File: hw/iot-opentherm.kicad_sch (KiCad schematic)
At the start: 32 parts, among them J1 USB_B_Micro, J2 Conn_01x02, J3 Conn_01x03, J4 Conn_02x06_Odd_Even, J5 Conn_01x02, Q1 BC858, U1 AMS1117-3.3, U2 ESP-12S, U3 PC817, U4 PC817

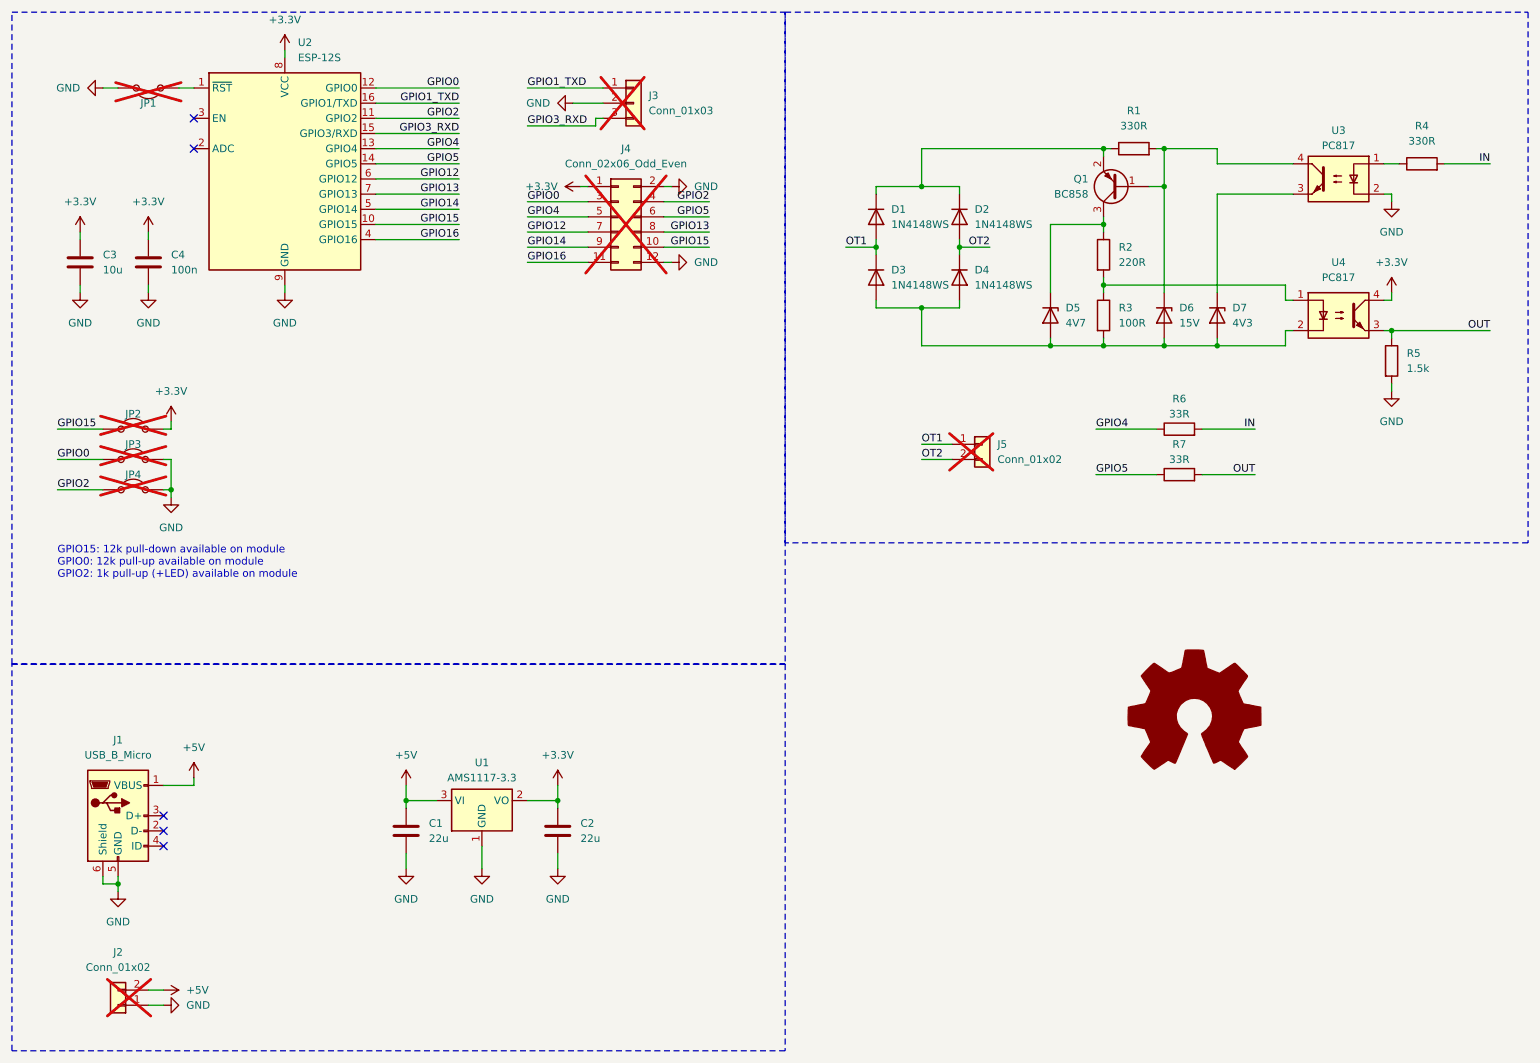
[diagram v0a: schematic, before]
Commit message: Fixes after running first version
1. Corrected footprint for D1, D2, D3, D4 to bigger one
2. Added connectors for OTx and +5VDC.
3. Added labels for OTx and +5VDC
4. ERC: no regression
5. DRC: two more issues
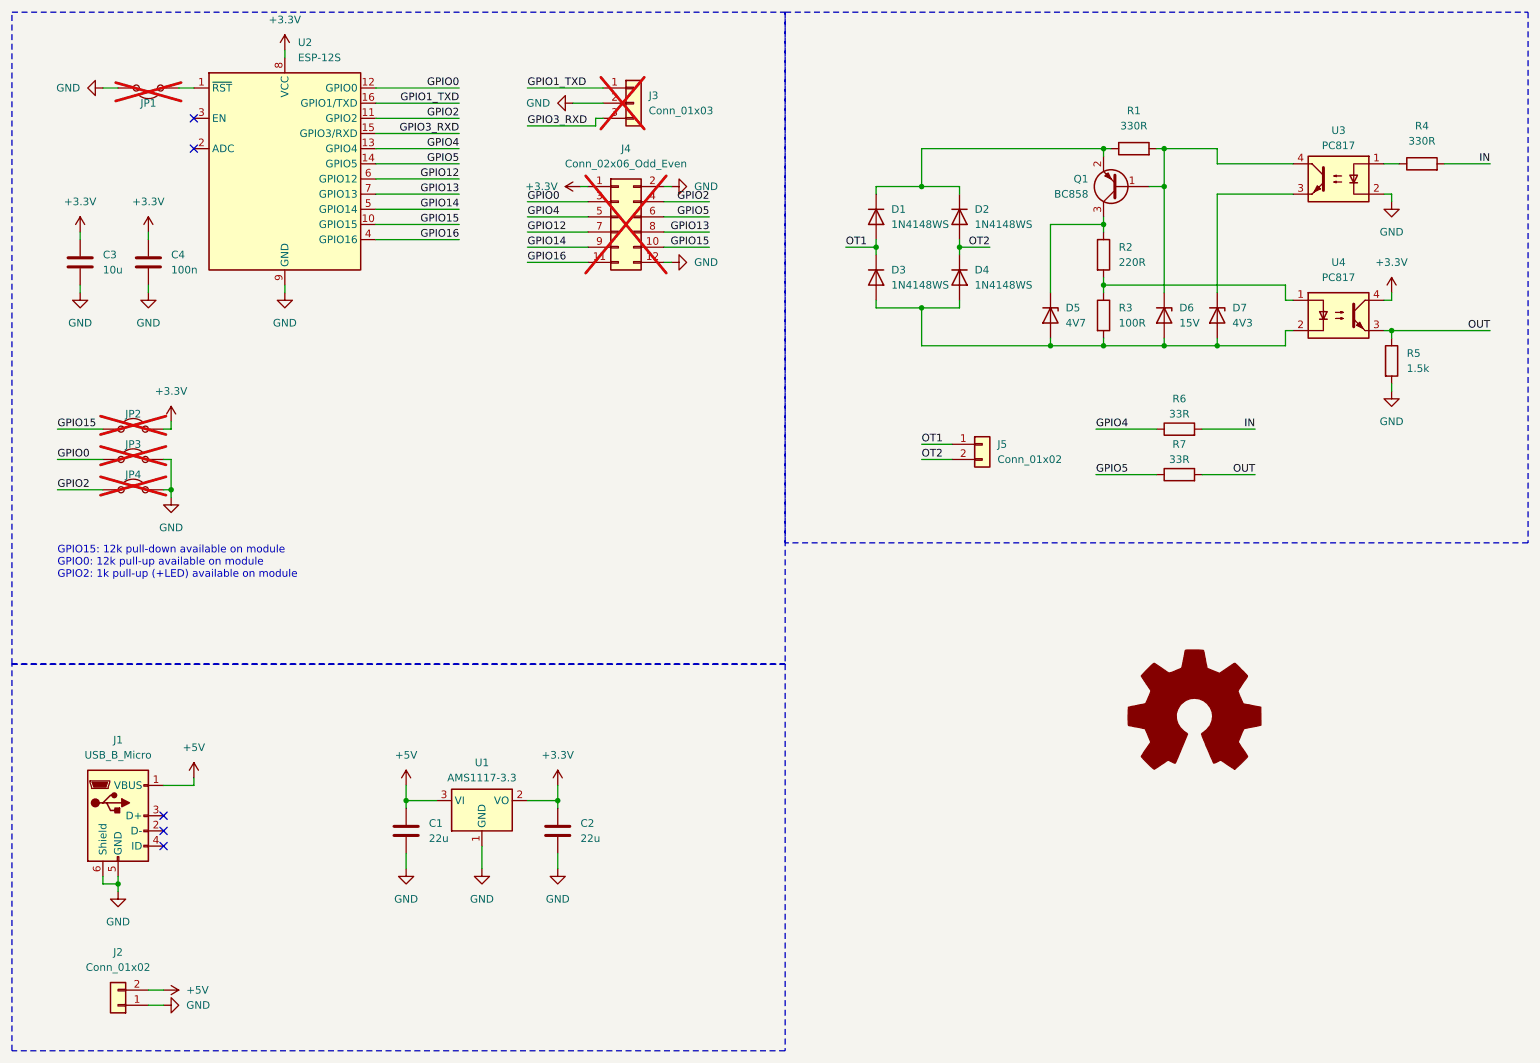
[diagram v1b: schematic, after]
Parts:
- D1, D2, D3, D4: footprint Diode_SMD:D_SOD-323 -> Diode_SMD:D_SOD-323_HandSoldering
- J2, J5: footprint Connector_PinHeader_2.54mm:PinHeader_1x02_P2.54mm_Vertical -> Connector_TE-Connectivity_:TE_282834-2; Farnell (none) -> 2112482; LCSC (none) -> C592983; Mouser (none) -> 571-282834-2; now fitted
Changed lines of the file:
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@@
 		(title "IoT OpenTherm")
 		(date "2024-10-07")
-		(rev "1.00")
+		(rev "1.01")
 		(company "Elezbyl")
 	)
@@
 		(in_bom yes)
 		(on_board yes)
-		(dnp yes)
+		(dnp no)
 		(fields_autoplaced yes)
 		(property "Reference" "J5"
@@
 			)
 		)
-		(property "Footprint" "Connector_PinHeader_2.54mm:PinHeader_1x02_P2.54mm_Vertical"
+		(property "Footprint" "Connector_TE-Connectivity_:TE_282834-2"
 			(at 186.69 90.17 0)
 			(effects
@@
 			)
 		)
+		(property "LCSC" "C592983"
+			(at 186.69 90.17 0)
+			(effects
+				(font
+					(size 1.27 1.27)
+				)
+				(hide yes)
+			)
+		)
+		(property "Farnell" "2112482"
+			(at 186.69 90.17 0)
+			(effects
+				(font
+					(size 1.27 1.27)
+				)
+				(hide yes)
+			)
+		)
+		(property "Mouser" "571-282834-2"
+			(at 186.69 90.17 0)
+			(effects
+				(font
+					(size 1.27 1.27)
+				)
+				(hide yes)
+			)
+		)
 		(pin "1"
 		)
@@
 			)
 		)
-		(property "Footprint" "Diode_SMD:D_SOD-323"
+		(property "Footprint" "Diode_SMD:D_SOD-323_HandSoldering"
 			(at 178.435 62.23 0)
 			(effects
@@
 			)
 		)
-		(property "Footprint" "Diode_SMD:D_SOD-323"
+		(property "Footprint" "Diode_SMD:D_SOD-323_HandSoldering"
 			(at 164.465 62.23 0)
 			(effects
@@
 		(in_bom yes)
 		(on_board yes)
-		(dnp yes)
+		(dnp no)
 		(fields_autoplaced yes)
 		(property "Reference" "J2"
@@
 			)
 		)
-		(property "Footprint" "Connector_PinHeader_2.54mm:PinHeader_1x02_P2.54mm_Vertical"
+		(property "Footprint" "Connector_TE-Connectivity_:TE_282834-2"
 			(at 41.91 184.15 0)
 			(effects
@@
 			)
 		)
+		(property "LCSC" "C592983"
+			(at 41.91 184.15 0)
+			(effects
+				(font
+					(size 1.27 1.27)
+				)
+				(hide yes)
+			)
+		)
+		(property "Farnell" "2112482"
+			(at 41.91 184.15 0)
+			(effects
+				(font
+					(size 1.27 1.27)
+				)
+				(hide yes)
+			)
+		)
+		(property "Mouser" "571-282834-2"
+			(at 41.91 184.15 0)
+			(effects
+				(font
+					(size 1.27 1.27)
+				)
+				(hide yes)
+			)
+		)
 		(pin "1"
 		)
@@
 			)
 		)
-		(property "Footprint" "Diode_SMD:D_SOD-323"
+		(property "Footprint" "Diode_SMD:D_SOD-323_HandSoldering"
 			(at 178.435 52.07 0)
 			(effects
@@
 			)
 		)
-		(property "Footprint" "Diode_SMD:D_SOD-323"
+		(property "Footprint" "Diode_SMD:D_SOD-323_HandSoldering"
 			(at 164.465 52.07 0)
 			(effects
